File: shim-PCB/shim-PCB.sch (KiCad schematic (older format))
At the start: 22 parts, among them J1 ROMI-Encoder, J10 LineSensor, J11 LineSensor, J12 SPI, J13 Ultrasonic., J14 THING, J15 THING, J2 ROMI-Encoder, J3 PROBE-POINT, J4 ServoAnalog, J5 Conn_02x15_Odd_Even, J6 ESP-DEVKITC, J7 ROMI, J8 ROMI, J9 PROBE-POINT

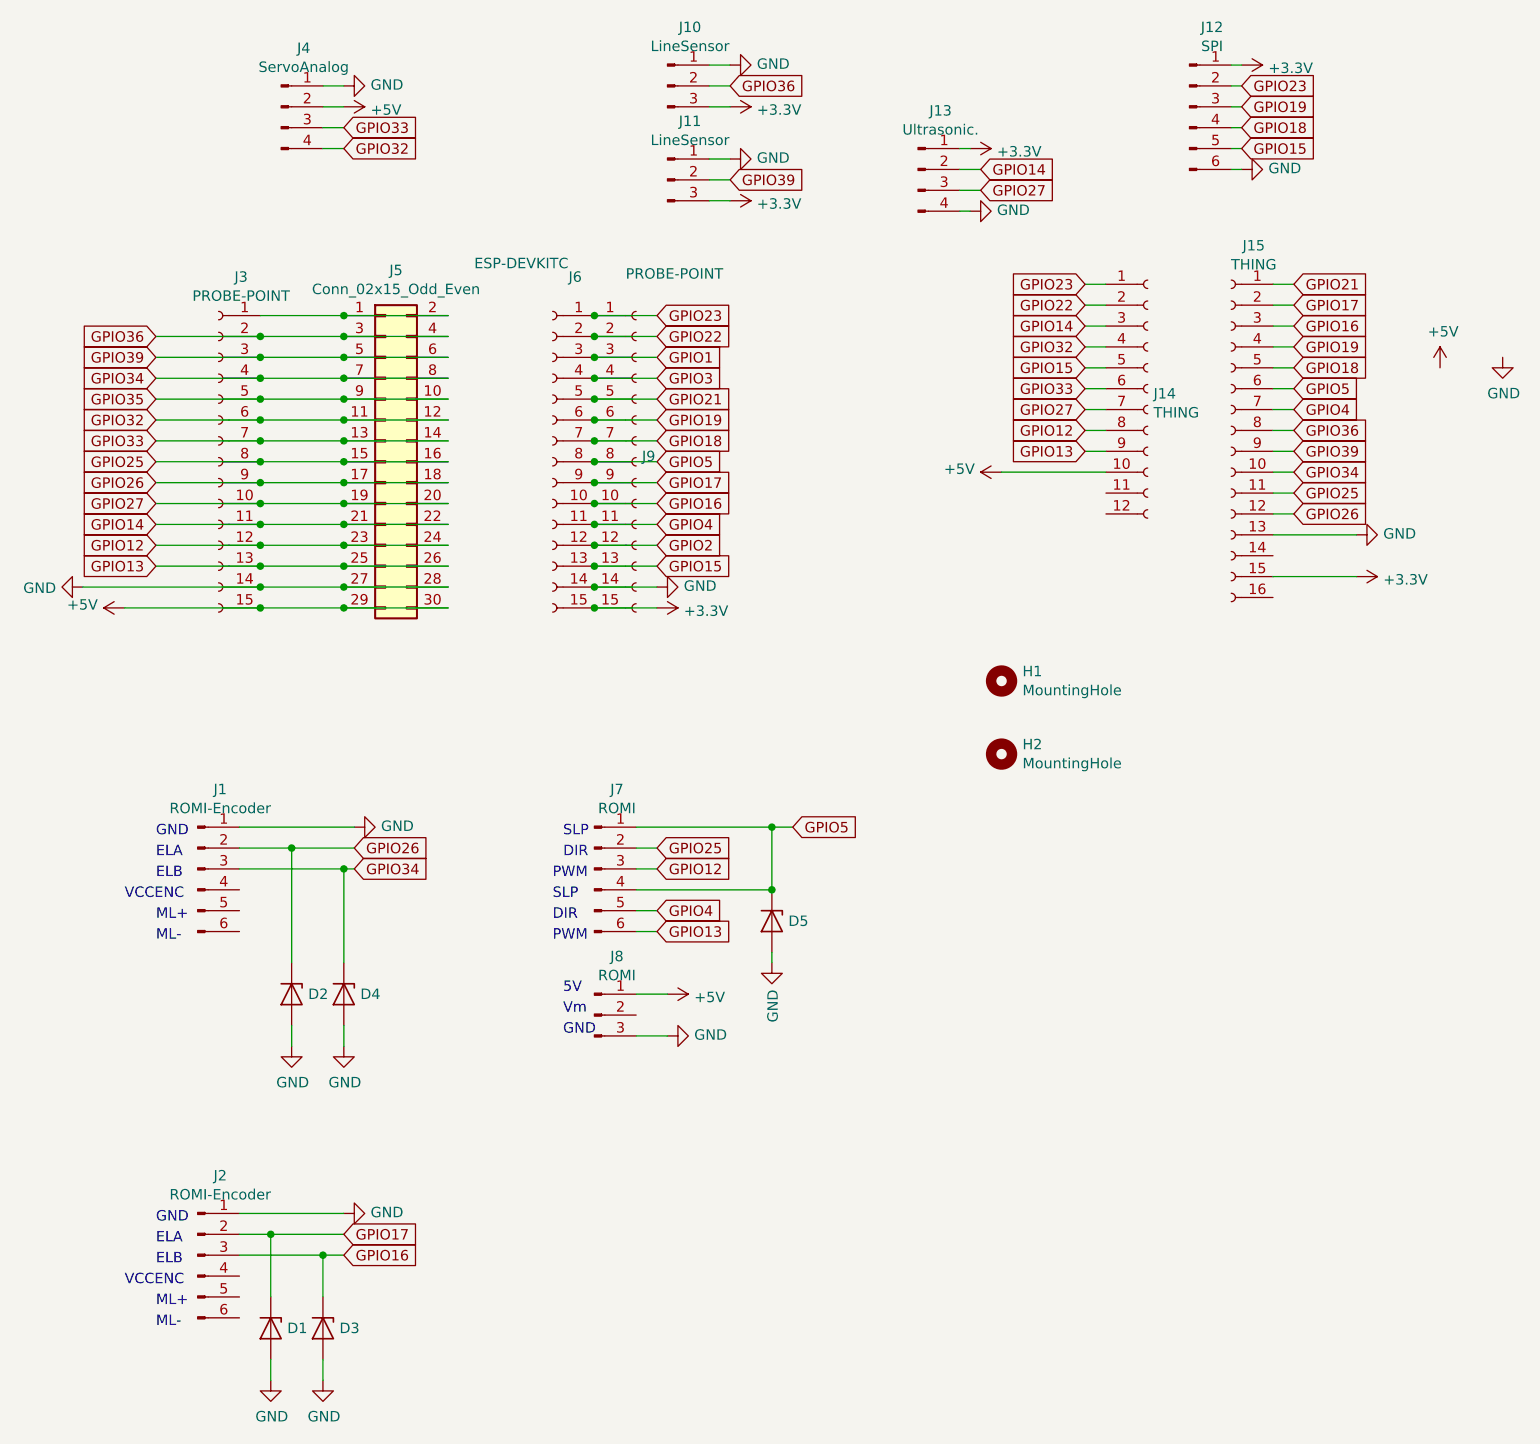
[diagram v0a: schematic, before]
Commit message: Swapped out esp32 devkit for v4
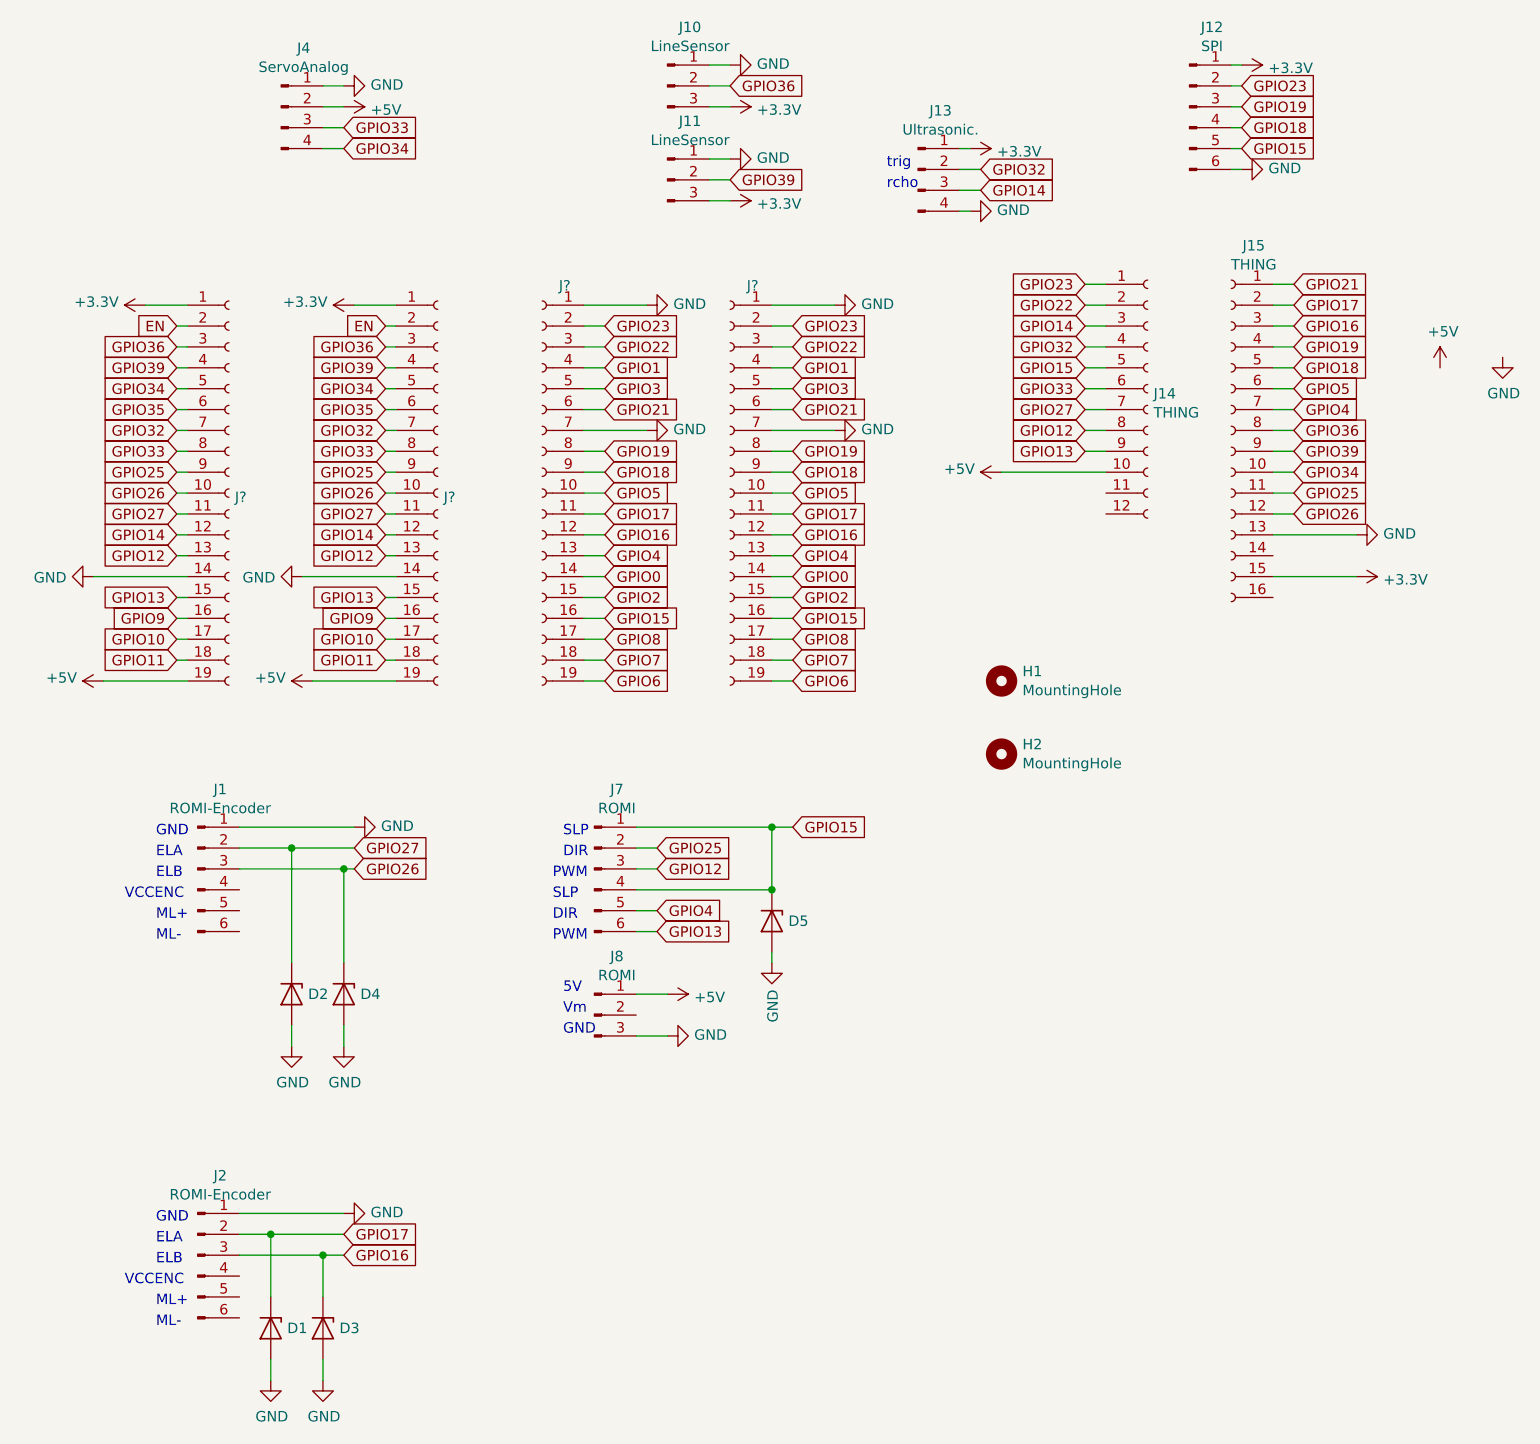
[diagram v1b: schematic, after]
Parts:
- removed J3, J9: PROBE-POINT, Connector_PinSocket_2.54mm:PinSocket_1x15_P2.54mm_Vertical, symbol Connector:Conn_01x15_Female
- removed J5: Conn_02x15_Odd_Even, Connector_PinSocket_2.54mm:PinSocket_2x15_P2.54mm_Vertical, symbol Connector_Generic:Conn_02x15_Odd_Even
- removed J6: ESP-DEVKITC, Connector_PinSocket_2.54mm:PinSocket_1x15_P2.54mm_Vertical, symbol Connector:Conn_01x15_Female
- added J? (x4): Conn_01x19_Female, symbol Connector:Conn_01x19_Female
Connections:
- net +3V3: now also J?.1 (Pin_1), J?.1 (Pin_1)
- net +5V: now also J?.19 (Pin_19), J?.19 (Pin_19)
- net GND: now also J?.1 (Pin_1), J?.1 (Pin_1), J?.14 (Pin_14), J?.14 (Pin_14), J?.7 (Pin_7), J?.7 (Pin_7)
- net GPIO1: now also J?.4 (Pin_4), J?.4 (Pin_4)
- net GPIO12: now also J?.13 (Pin_13), J?.13 (Pin_13)
- net GPIO13: now also J?.15 (Pin_15), J?.15 (Pin_15)
- net GPIO14: now also J13.3 (Pin_3), J?.12 (Pin_12), J?.12 (Pin_12); no longer J13.2 (Pin_2)
- net GPIO15: now also D5.1 (K), J7.1 (Pin_1), J7.4 (Pin_4), J?.16 (Pin_16), J?.16 (Pin_16)
- net GPIO16: now also J?.12 (Pin_12), J?.12 (Pin_12)
- net GPIO17: now also J?.11 (Pin_11), J?.11 (Pin_11)
- net GPIO18: now also J?.9 (Pin_9), J?.9 (Pin_9)
- net GPIO19: now also J?.8 (Pin_8), J?.8 (Pin_8)
- net GPIO2: now also J?.15 (Pin_15), J?.15 (Pin_15)
- net GPIO21: now also J?.6 (Pin_6), J?.6 (Pin_6)
- net GPIO22: now also J?.3 (Pin_3), J?.3 (Pin_3)
- net GPIO23: now also J?.2 (Pin_2), J?.2 (Pin_2)
- net GPIO25: now also J?.9 (Pin_9), J?.9 (Pin_9)
- net GPIO26: now also D4.1 (K), J1.3 (Pin_3), J?.10 (Pin_10), J?.10 (Pin_10); no longer D2.1 (K), J1.2 (Pin_2)
- net GPIO27: now also D2.1 (K), J1.2 (Pin_2), J?.11 (Pin_11), J?.11 (Pin_11); no longer J13.3 (Pin_3)
- net GPIO3: now also J?.5 (Pin_5), J?.5 (Pin_5)
- net GPIO32: now also J13.2 (Pin_2), J?.7 (Pin_7), J?.7 (Pin_7); no longer J4.4 (Pin_4)
- net GPIO33: now also J?.8 (Pin_8), J?.8 (Pin_8)
- net GPIO34: now also J4.4 (Pin_4), J?.5 (Pin_5), J?.5 (Pin_5); no longer D4.1 (K), J1.3 (Pin_3)
- net GPIO35: now also J?.6 (Pin_6), J?.6 (Pin_6)
- net GPIO36: now also J?.3 (Pin_3), J?.3 (Pin_3)
- net GPIO39: now also J?.4 (Pin_4), J?.4 (Pin_4)
- net GPIO4: now also J?.13 (Pin_13), J?.13 (Pin_13)
- net GPIO5: now also J?.10 (Pin_10), J?.10 (Pin_10); no longer D5.1 (K), J7.1 (Pin_1), J7.4 (Pin_4)
- new net EN: J?.2 (Pin_2), J?.2 (Pin_2)
- new net GPIO0: J?.14 (Pin_14), J?.14 (Pin_14)
- new net GPIO10: J?.17 (Pin_17), J?.17 (Pin_17)
- new net GPIO11: J?.18 (Pin_18), J?.18 (Pin_18)
- new net GPIO6: J?.19 (Pin_19), J?.19 (Pin_19)
- new net GPIO7: J?.18 (Pin_18), J?.18 (Pin_18)
- new net GPIO8: J?.17 (Pin_17), J?.17 (Pin_17)
- new net GPIO9: J?.16 (Pin_16), J?.16 (Pin_16)
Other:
- note added: "rcho"
- note added: "trig"

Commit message: Clamped ~SLP pin and added 02x01 header.
Issue #13
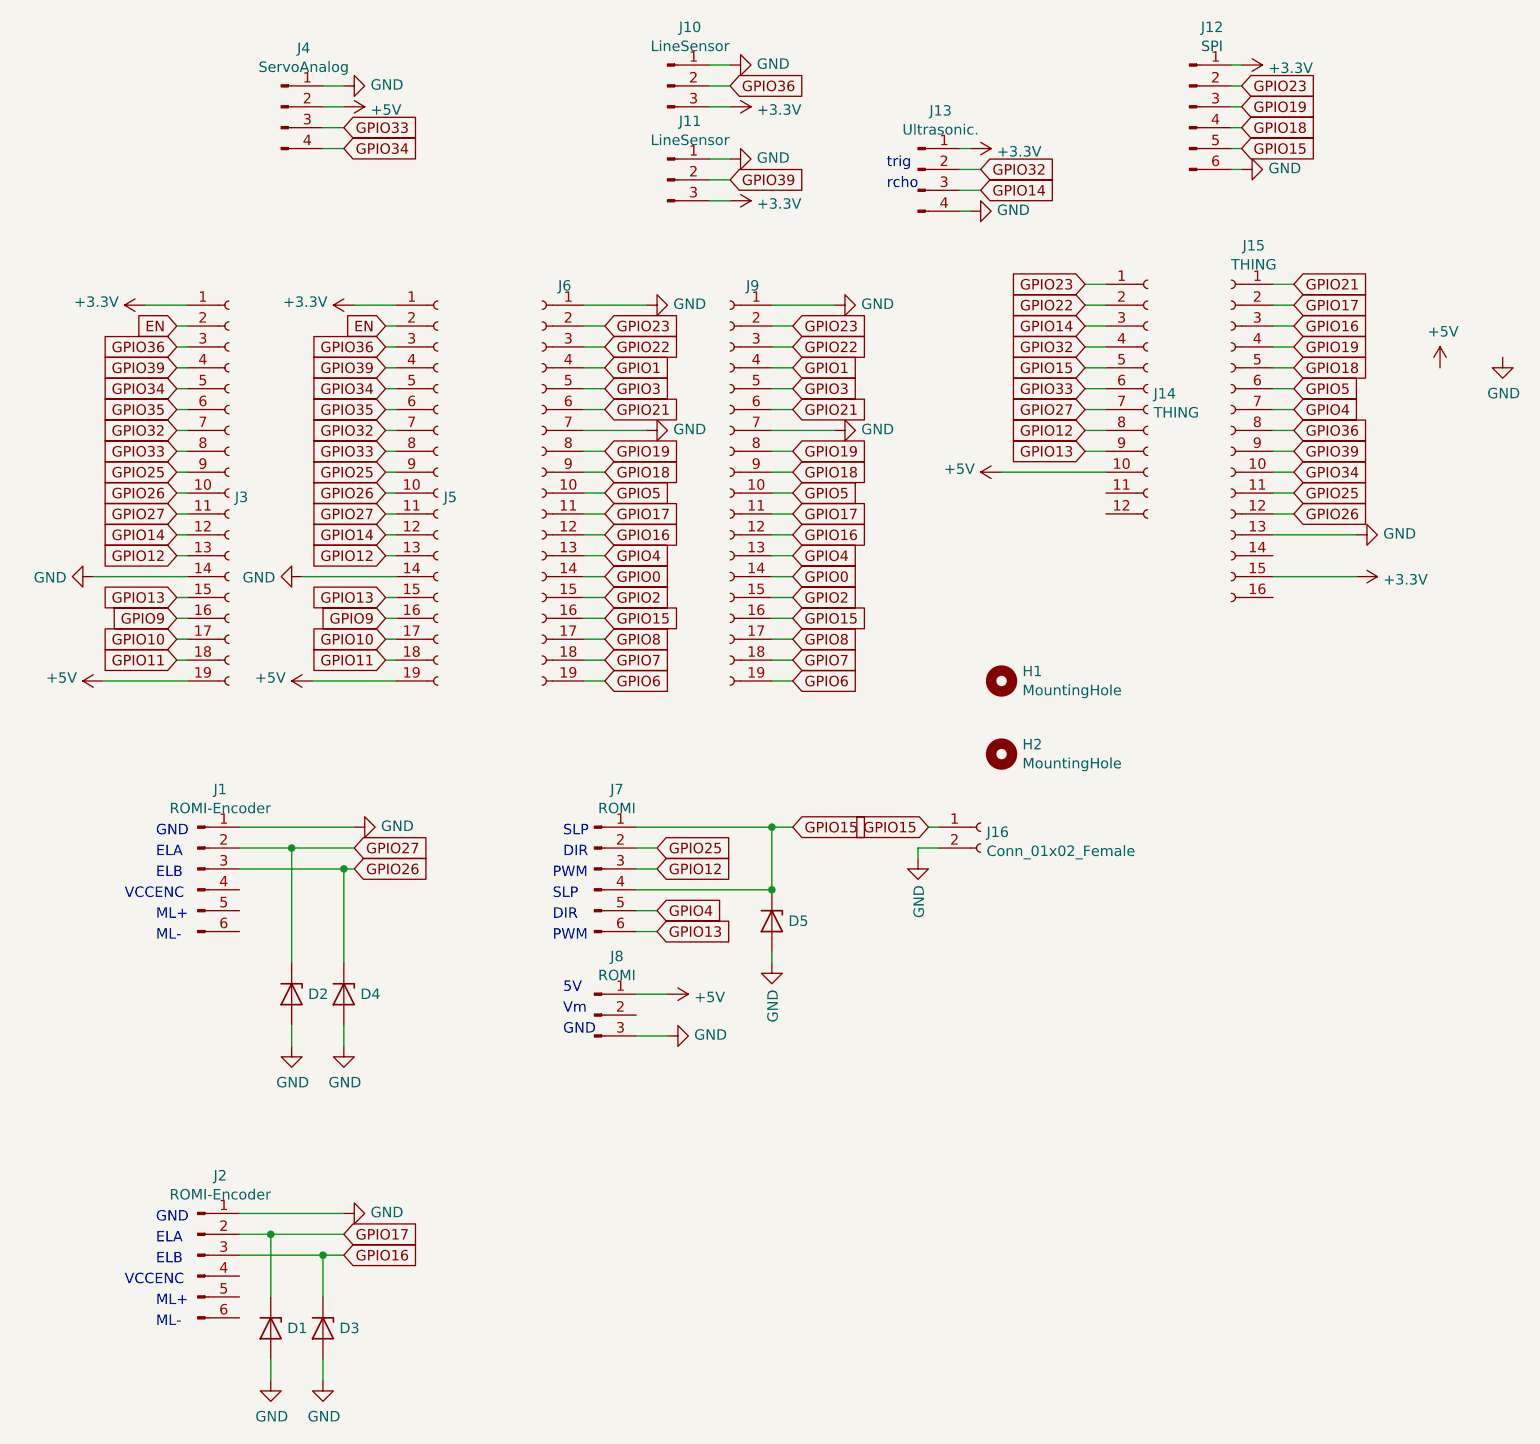
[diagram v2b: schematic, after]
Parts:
- added J16: Conn_01x02_Female, Connector_PinSocket_2.54mm:PinSocket_1x02_P2.54mm_Vertical, symbol Connector:Conn_01x02_Female
- J3, J5, J6, J9: renamed from J?; footprint (none) -> Connector_PinSocket_2.54mm:PinSocket_1x19_P2.54mm_Vertical
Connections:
- net GND: now also J16.2 (Pin_2)
- net GPIO15: now also J16.1 (Pin_1)
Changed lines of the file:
@@
 rcho
 $Comp
-L Connector:Conn_01x19_Female J?
+L Connector:Conn_01x19_Female J5
 U 1 1 5F01D059
 P 2500 2950
-F 0 "J?" H 2528 2930 50  0000 L CNN
+F 0 "J5" H 2528 2930 50  0000 L CNN
 F 1 "Conn_01x19_Female" H 2528 2885 50  0001 L CNN
-F 2 "" H 2500 2950 50  0001 C CNN
+F 2 "Connector_PinSocket_2.54mm:PinSocket_1x19_P2.54mm_Vertical" H 2500 2950 50  0001 C CNN
 F 3 "~" H 2500 2950 50  0001 C CNN
 	1    2500 2950
@@
 $EndComp
 $Comp
-L Connector:Conn_01x19_Female J?
+L Connector:Conn_01x19_Female J6
 U 1 1 5F01FD46
 P 3000 2950
-F 0 "J?" H 2892 3943 50  0000 C CNN
+F 0 "J6" H 2892 3943 50  0000 C CNN
 F 1 "Conn_01x19_Female" H 2892 3944 50  0001 C CNN
-F 2 "" H 3000 2950 50  0001 C CNN
+F 2 "Connector_PinSocket_2.54mm:PinSocket_1x19_P2.54mm_Vertical" H 3000 2950 50  0001 C CNN
 F 3 "~" H 3000 2950 50  0001 C CNN
 	1    3000 2950
@@
 $EndComp
 $Comp
-L power:+3.3V #PWR?
+L power:+3.3V #PWR0106
 U 1 1 5F044560
 P 2100 2050
-F 0 "#PWR?" H 2100 1900 50  0001 C CNN
+F 0 "#PWR0106" H 2100 1900 50  0001 C CNN
 F 1 "+3.3V" V 2115 2178 50  0000 L CNN
 F 2 "" H 2100 2050 50  0001 C CNN
@@
 GPIO12
 $Comp
-L power:GND #PWR?
+L power:GND #PWR0107
 U 1 1 5F04AAFB
 P 1850 3350
-F 0 "#PWR?" H 1850 3100 50  0001 C CNN
+F 0 "#PWR0107" H 1850 3100 50  0001 C CNN
 F 1 "GND" V 1855 3222 50  0000 R CNN
 F 2 "" H 1850 3350 50  0001 C CNN
@@
 GPIO11
 $Comp
-L power:+5V #PWR?
+L power:+5V #PWR0108
 U 1 1 5F04D5C5
 P 1900 3850
-F 0 "#PWR?" H 1900 3700 50  0001 C CNN
+F 0 "#PWR0108" H 1900 3700 50  0001 C CNN
 F 1 "+5V" V 1915 3978 50  0000 L CNN
 F 2 "" H 1900 3850 50  0001 C CNN
@@
 	1850 3350 2300 3350
 $Comp
-L power:GND #PWR?
+L power:GND #PWR0109
 U 1 1 5F0613E4
 P 3500 2050
-F 0 "#PWR?" H 3500 1800 50  0001 C CNN
+F 0 "#PWR0109" H 3500 1800 50  0001 C CNN
 F 1 "GND" V 3505 1922 50  0000 R CNN
 F 2 "" H 3500 2050 50  0001 C CNN
@@
 GPIO6
 $Comp
-L power:GND #PWR?
+L power:GND #PWR0129
 U 1 1 5F072993
 P 3500 2650
-F 0 "#PWR?" H 3500 2400 50  0001 C CNN
+F 0 "#PWR0129" H 3500 2400 50  0001 C CNN
 F 1 "GND" V 3505 2522 50  0000 R CNN
 F 2 "" H 3500 2650 50  0001 C CNN
@@
 	2300 2150 2250 2150
 $Comp
-L Connector:Conn_01x19_Female J?
+L Connector:Conn_01x19_Female J3
 U 1 1 5F2652BC
 P 1500 2950
-F 0 "J?" H 1528 2930 50  0000 L CNN
+F 0 "J3" H 1528 2930 50  0000 L CNN
 F 1 "Conn_01x19_Female" H 1528 2885 50  0001 L CNN
-F 2 "" H 1500 2950 50  0001 C CNN
+F 2 "Connector_PinSocket_2.54mm:PinSocket_1x19_P2.54mm_Vertical" H 1500 2950 50  0001 C CNN
 F 3 "~" H 1500 2950 50  0001 C CNN
 	1    1500 2950
@@
 $EndComp
 $Comp
-L power:+3.3V #PWR?
+L power:+3.3V #PWR0130
 U 1 1 5F2652C2
 P 1100 2050
-F 0 "#PWR?" H 1100 1900 50  0001 C CNN
+F 0 "#PWR0130" H 1100 1900 50  0001 C CNN
 F 1 "+3.3V" V 1115 2178 50  0000 L CNN
 F 2 "" H 1100 2050 50  0001 C CNN
@@
 GPIO12
 $Comp
-L power:GND #PWR?
+L power:GND #PWR0131
 U 1 1 5F2652D3
 P 850 3350
-F 0 "#PWR?" H 850 3100 50  0001 C CNN
+F 0 "#PWR0131" H 850 3100 50  0001 C CNN
 F 1 "GND" V 855 3222 50  0000 R CNN
 F 2 "" H 850 3350 50  0001 C CNN
@@
 GPIO11
 $Comp
-L power:+5V #PWR?
+L power:+5V #PWR0132
 U 1 1 5F2652DD
 P 900 3850
-F 0 "#PWR?" H 900 3700 50  0001 C CNN
+F 0 "#PWR0132" H 900 3700 50  0001 C CNN
 F 1 "+5V" V 915 3978 50  0000 L CNN
 F 2 "" H 900 3850 50  0001 C CNN
@@
 	1300 2150 1250 2150
 $Comp
-L Connector:Conn_01x19_Female J?
+L Connector:Conn_01x19_Female J9
 U 1 1 5F2A4CB9
 P 3900 2950
-F 0 "J?" H 3792 3943 50  0000 C CNN
+F 0 "J9" H 3792 3943 50  0000 C CNN
 F 1 "Conn_01x19_Female" H 3792 3944 50  0001 C CNN
-F 2 "" H 3900 2950 50  0001 C CNN
+F 2 "Connector_PinSocket_2.54mm:PinSocket_1x19_P2.54mm_Vertical" H 3900 2950 50  0001 C CNN
 F 3 "~" H 3900 2950 50  0001 C CNN
 	1    3900 2950
@@
 $EndComp
 $Comp
-L power:GND #PWR?
+L power:GND #PWR0133
 U 1 1 5F2A4CBF
 P 4400 2050
-F 0 "#PWR?" H 4400 1800 50  0001 C CNN
+F 0 "#PWR0133" H 4400 1800 50  0001 C CNN
 F 1 "GND" V 4405 1922 50  0000 R CNN
 F 2 "" H 4400 2050 50  0001 C CNN
@@
 GPIO6
 $Comp
-L power:GND #PWR?
+L power:GND #PWR0134
 U 1 1 5F2A4CD6
 P 4400 2650
-F 0 "#PWR?" H 4400 2400 50  0001 C CNN
+F 0 "#PWR0134" H 4400 2400 50  0001 C CNN
 F 1 "GND" V 4405 2522 50  0000 R CNN
 F 2 "" H 4400 2650 50  0001 C CNN
@@
 Wire Wire Line
 	4200 3850 4100 3850
+$Comp
+L Connector:Conn_01x02_Female J16
+U 1 1 5F30E014
+P 5100 4550
+F 0 "J16" H 5128 4526 50  0000 L CNN
+F 1 "Conn_01x02_Female" H 5128 4435 50  0000 L CNN
+F 2 "Connector_PinSocket_2.54mm:PinSocket_1x02_P2.54mm_Vertical" H 5100 4550 50  0001 C CNN
+F 3 "~" H 5100 4550 50  0001 C CNN
+	1    5100 4550
+	1    0    0    -1
+$EndComp
+Text GLabel 4850 4550 0    50   Input ~ 0
+GPIO15
+$Comp
+L power:GND #PWR0135
+U 1 1 5F30EFD3
+P 4800 4700
+F 0 "#PWR0135" H 4800 4450 50  0001 C CNN
+F 1 "GND" V 4805 4572 50  0000 R CNN
+F 2 "" H 4800 4700 50  0001 C CNN
+F 3 "" H 4800 4700 50  0001 C CNN
+	1    4800 4700
+	1    0    0    -1
+$EndComp
+Wire Wire Line
+	4900 4550 4850 4550
+Wire Wire Line
+	4900 4650 4800 4650
+Wire Wire Line
+	4800 4650 4800 4700
 $EndSCHEMATC
